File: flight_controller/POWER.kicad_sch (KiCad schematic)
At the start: 0 parts

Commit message: gps and power blocks
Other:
- note added: "15135-0801 cabel"
- note added: "JST B8B-PH-SM4-TBT(LF)(SN) CONN 8 PIN"
- note added: "MOLEX 5024430860 conn 8 pin"
- note added: "cabel ???"

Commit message: cleanup and improvements
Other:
- note added: "???"
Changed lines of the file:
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@@
+		)
+	)
+	(text "???"
+		(exclude_from_sim no)
+		(at 157.226 118.11 0)
+		(effects
+			(font
+				(size 1.27 1.27)
+			)
 		)
 	)
@@
 	(wire
 		(pts
+			(xy 123.19 123.19) (xy 158.75 123.19)
+		)
+		(stroke
+			(width 0)
+			(type default)
+			(color 255 0 0 1)
+		)
+	)
+	(wire
+		(pts
 			(xy 129.54 77.47) (xy 129.54 80.01)
 		)
@@
 			(width 0)
 			(type default)
+		)
+	)
+	(label "USB_TYPE_C_SENSE"
+		(at 132.08 123.19 0)
+		(effects
+			(font
+				(size 1.27 1.27)
+			)
+			(justify left bottom)
 		)
 	)
@@
 		(effects
 			(font
+				(size 1.27 1.27)
+			)
+			(justify left)
+		)
+	)
+	(hierarchical_label "USB_TYPE_C_SENSE"
+		(shape output)
+		(at 158.75 123.19 0)
+		(effects
+			(font

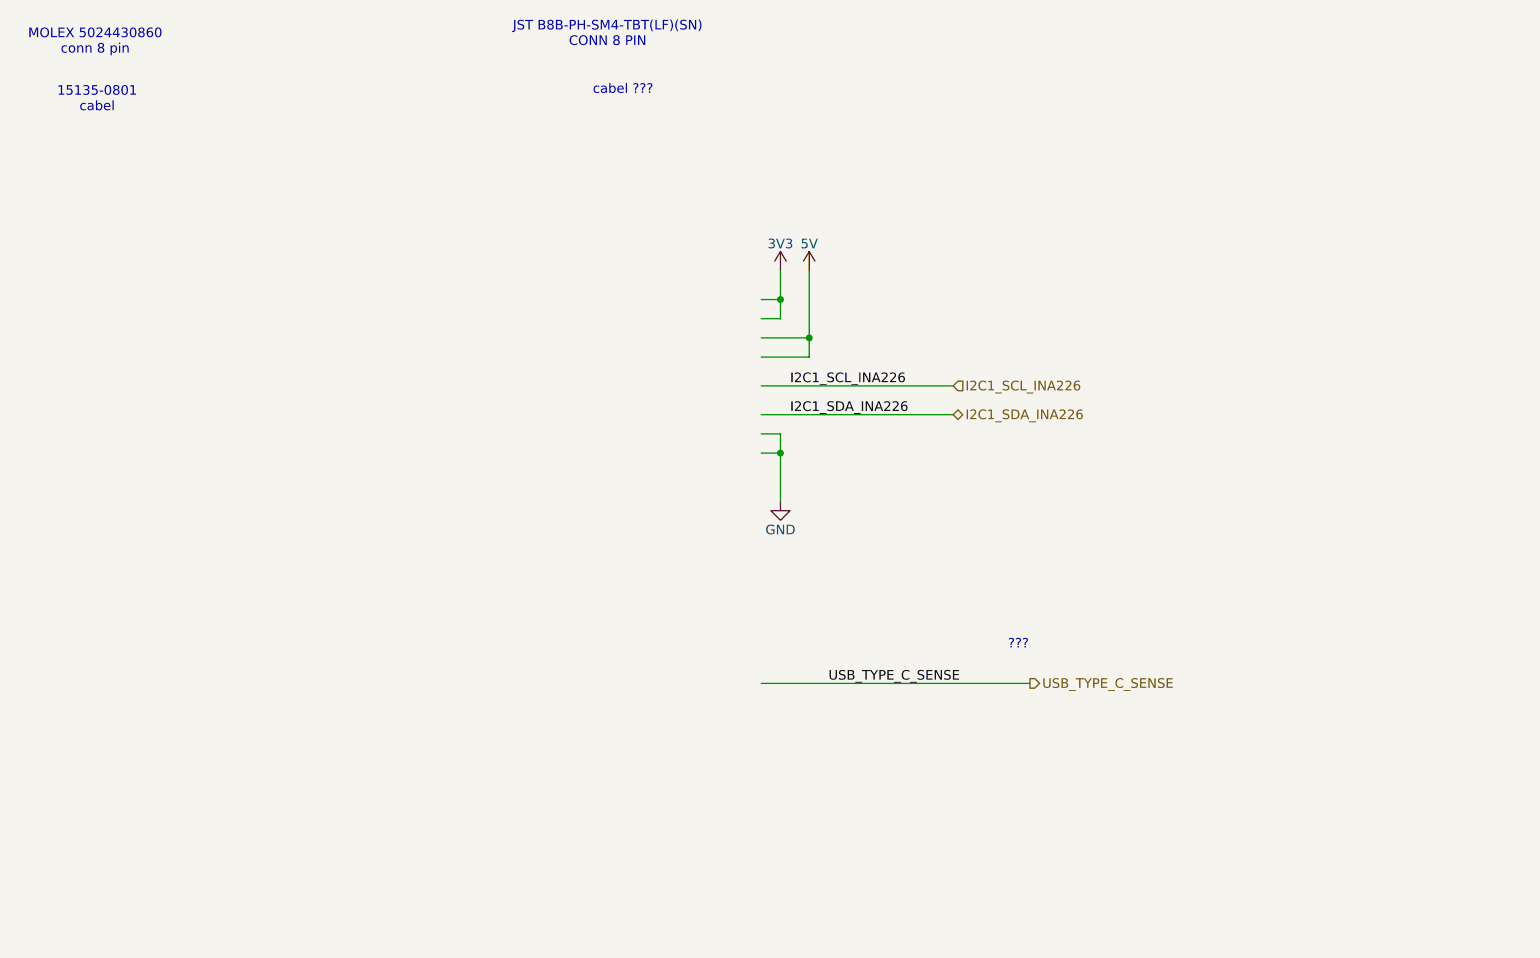
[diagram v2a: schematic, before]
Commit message: Schematic complete, ready for layout. Added USB, TPs, power conn, updated clocks, ran Rules Checker and general review
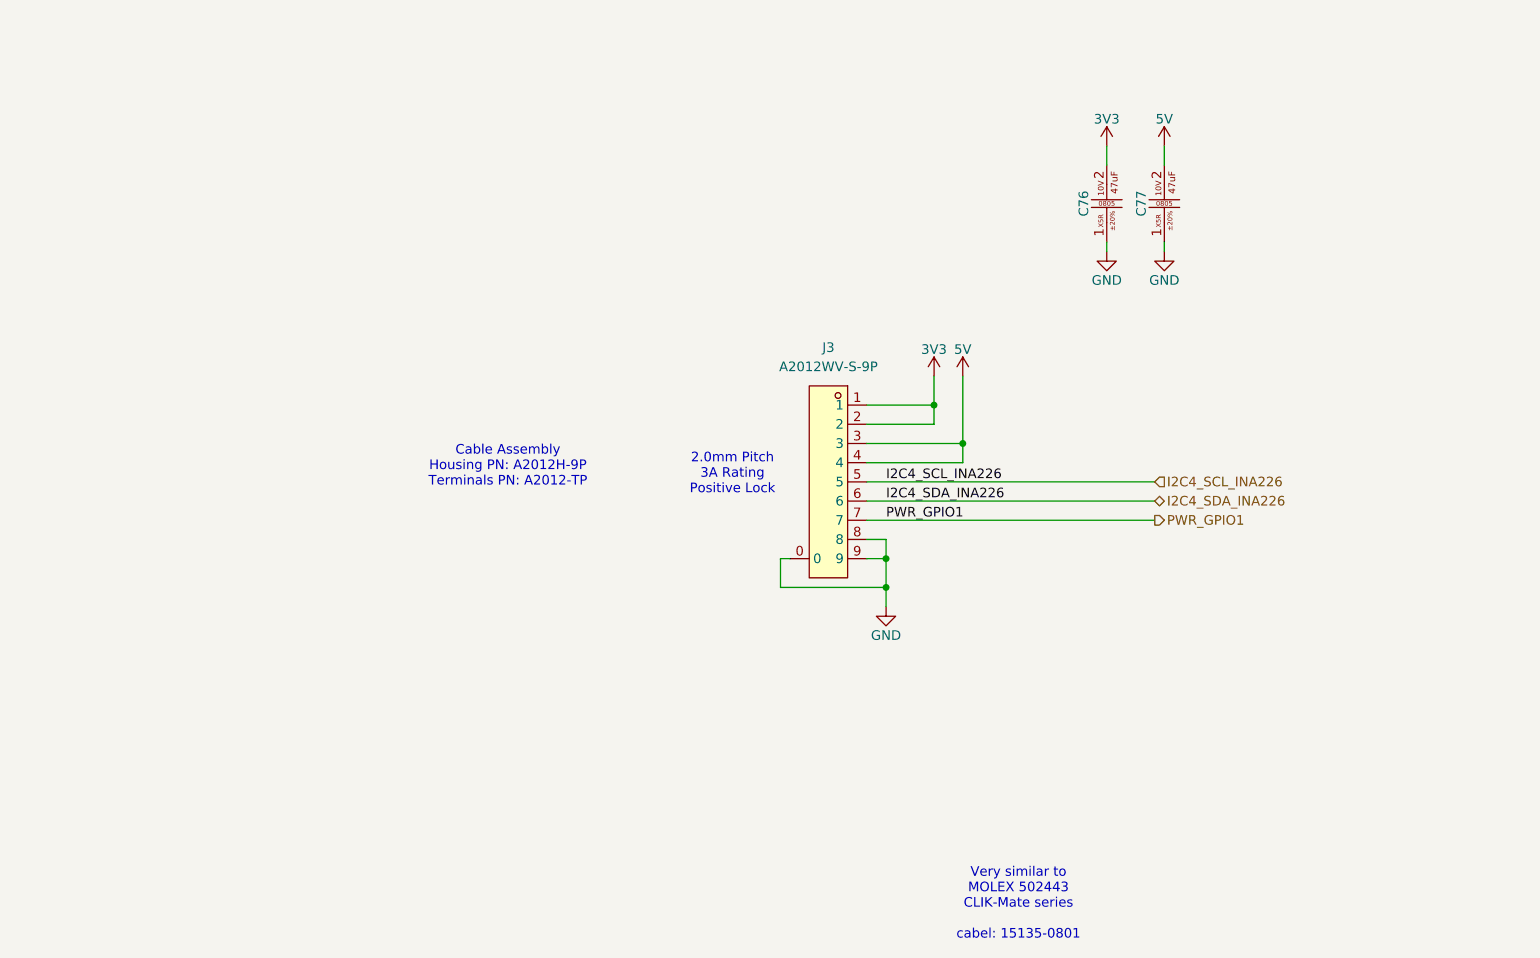
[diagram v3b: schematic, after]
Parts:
- added C76, C77: GRM21BR61A476ME15L (47uF , 0805 ,10V ,X5R), easyeda2kicad:C0805, symbol lampelKicadLIB:GRM21BR61A476ME15L (47uF , 0805 ,10V ,X5R)
- added J3: A2012WV-S-9P, easyeda2kicad:CONN-SMD_A2012WV-S-9P, symbol lampelKicadLIB:A2012WV-S-9P
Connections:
- net 3V3: now also C76.2, J3.1, J3.2
- net 5V: now also C77.2, J3.3, J3.4
- net GND: now also C76.1, C77.1, J3.0, J3.8, J3.9
- new net I2C4_SCL_INA226: J3.5
- new net I2C4_SDA_INA226: J3.6
- new net PWR_GPIO1: J3.7
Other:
- note added: "2.0mm Pitch 3A Rating Positive Lock"
- note added: "Cable Assembly Housing PN: A2012H-9P Terminals PN: A2012-TP"
- note added: "Very similar to MOLEX 502443 CLIK-Mate series cabel: 15135-0801"
- note removed: "15135-0801 cabel"
- note removed: "???"
- note removed: "JST B8B-PH-SM4-TBT(LF)(SN) CONN 8 PIN"
- note removed: "MOLEX 5024430860 conn 8 pin"
- note removed: "cabel ???"

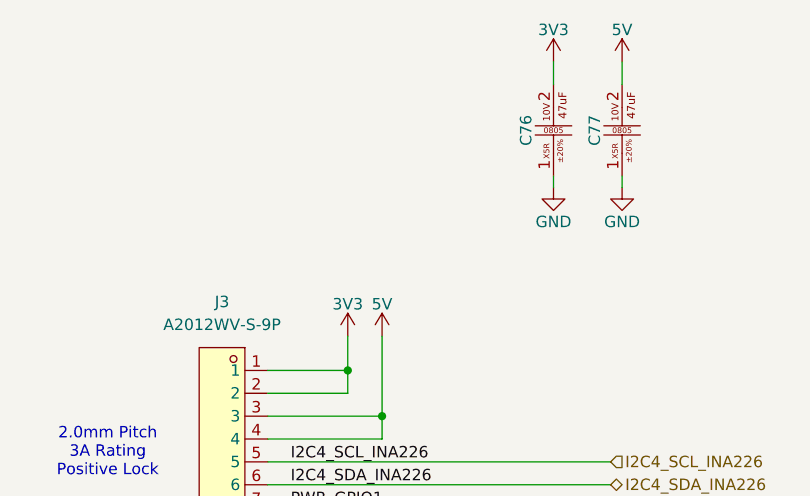
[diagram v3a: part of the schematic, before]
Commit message: Started the placement process
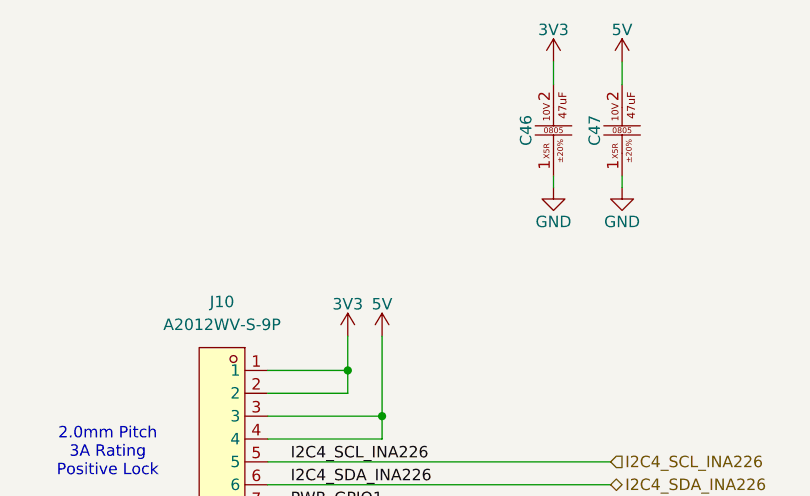
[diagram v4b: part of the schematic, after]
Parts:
- renumbered C76 to C46, C77 to C47, J3 to J10
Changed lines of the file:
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@@
 		(on_board yes)
 		(dnp no)
-		(property "Reference" "J3"
+		(property "Reference" "J10"
 			(at 132.08 78.74 0)
 			(effects
@@
 			(project ""
 				(path "/17737359-1a8e-4237-8899-d9604030bc1d/04e8a37e-c803-4b03-9bae-b305438bfc27"
-					(reference "J3")
+					(reference "J10")
 					(unit 1)
 				)
@@
 		(on_board yes)
 		(dnp no)
-		(property "Reference" "#PWR0128"
+		(property "Reference" "#PWR0118"
 			(at 139.7 119.38 0)
 			(effects
@@
 			(project "FP_BOARD"
 				(path "/17737359-1a8e-4237-8899-d9604030bc1d/04e8a37e-c803-4b03-9bae-b305438bfc27"
-					(reference "#PWR0128")
+					(reference "#PWR0118")
 					(unit 1)
 				)
@@
 		(dnp no)
 		(fields_autoplaced yes)
-		(property "Reference" "C77"
+		(property "Reference" "C47"
 			(at 173.482 59.69 0)
 			(do_not_autoplace yes)
@@
 			(project "FP_BOARD"
 				(path "/17737359-1a8e-4237-8899-d9604030bc1d/04e8a37e-c803-4b03-9bae-b305438bfc27"
-					(reference "C77")
+					(reference "C47")
 					(unit 1)
 				)
@@
 		(on_board yes)
 		(dnp no)
-		(property "Reference" "#PWR018"
+		(property "Reference" "#PWR0119"
 			(at 146.05 86.36 0)
 			(effects
@@
 			(project "FP_BOARD"
 				(path "/17737359-1a8e-4237-8899-d9604030bc1d/04e8a37e-c803-4b03-9bae-b305438bfc27"
-					(reference "#PWR018")
+					(reference "#PWR0119")
 					(unit 1)
 				)
@@
 		(on_board yes)
 		(dnp no)
-		(property "Reference" "#PWR085"
+		(property "Reference" "#PWR0120"
 			(at 149.86 86.36 0)
 			(effects
@@
 			(project "FP_BOARD"
 				(path "/17737359-1a8e-4237-8899-d9604030bc1d/04e8a37e-c803-4b03-9bae-b305438bfc27"
-					(reference "#PWR085")
+					(reference "#PWR0120")
 					(unit 1)
 				)
@@
 		(on_board yes)
 		(dnp no)
-		(property "Reference" "#PWR0134"
+		(property "Reference" "#PWR0124"
 			(at 176.53 72.39 0)
 			(effects
@@
 			(project "FP_BOARD"
 				(path "/17737359-1a8e-4237-8899-d9604030bc1d/04e8a37e-c803-4b03-9bae-b305438bfc27"
-					(reference "#PWR0134")
+					(reference "#PWR0124")
 					(unit 1)
 				)
@@
 		(dnp no)
 		(fields_autoplaced yes)
-		(property "Reference" "C76"
+		(property "Reference" "C46"
 			(at 165.862 59.69 0)
 			(do_not_autoplace yes)
@@
 			(project ""
 				(path "/17737359-1a8e-4237-8899-d9604030bc1d/04e8a37e-c803-4b03-9bae-b305438bfc27"
-					(reference "C76")
+					(reference "C46")
 					(unit 1)
 				)
@@
 		(on_board yes)
 		(dnp no)
-		(property "Reference" "#PWR0131"
+		(property "Reference" "#PWR0122"
 			(at 168.91 72.39 0)
 			(effects
@@
 			(project "FP_BOARD"
 				(path "/17737359-1a8e-4237-8899-d9604030bc1d/04e8a37e-c803-4b03-9bae-b305438bfc27"
-					(reference "#PWR0131")
+					(reference "#PWR0122")
 					(unit 1)
 				)
@@
 		(on_board yes)
 		(dnp no)
-		(property "Reference" "#PWR061"
+		(property "Reference" "#PWR0121"
 			(at 168.91 55.88 0)
 			(effects
@@
 			(project "FP_BOARD"
 				(path "/17737359-1a8e-4237-8899-d9604030bc1d/04e8a37e-c803-4b03-9bae-b305438bfc27"
-					(reference "#PWR061")
+					(reference "#PWR0121")
 					(unit 1)
 				)
@@
 		(on_board yes)
 		(dnp no)
-		(property "Reference" "#PWR0117"
+		(property "Reference" "#PWR0123"
 			(at 176.53 55.88 0)
 			(effects
@@
 			(project "FP_BOARD"
 				(path "/17737359-1a8e-4237-8899-d9604030bc1d/04e8a37e-c803-4b03-9bae-b305438bfc27"
-					(reference "#PWR0117")
-					(unit 1)
-				)
+					(reference "#PWR0123")
+					(unit 1)
+				)

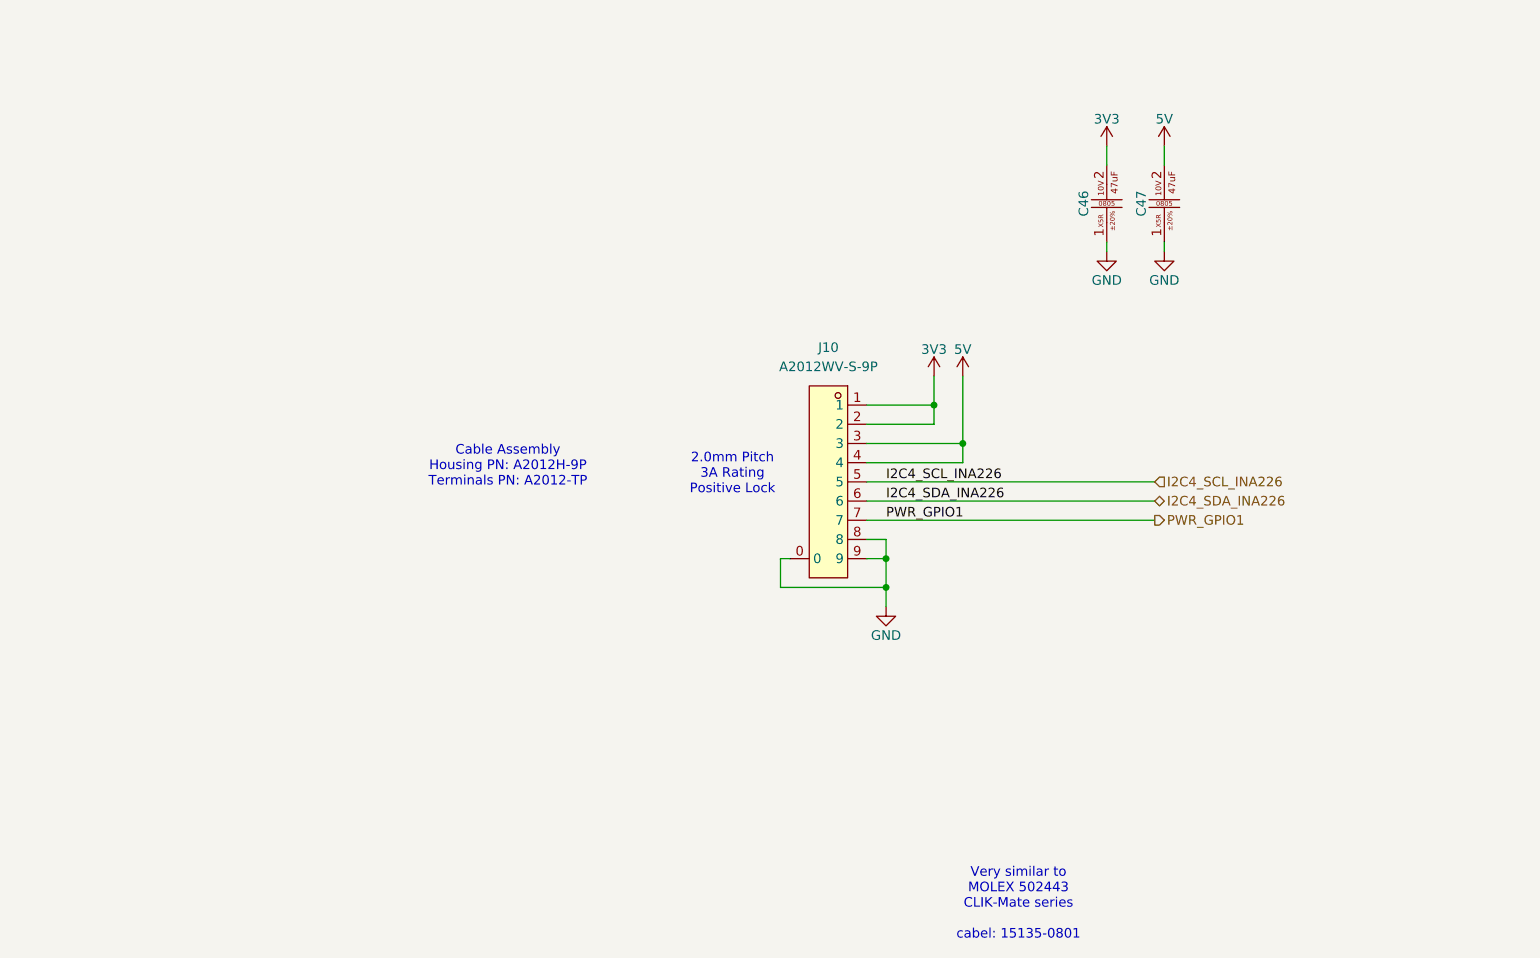
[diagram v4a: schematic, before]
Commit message: Updated power and usb connectors, annotations and netlist check
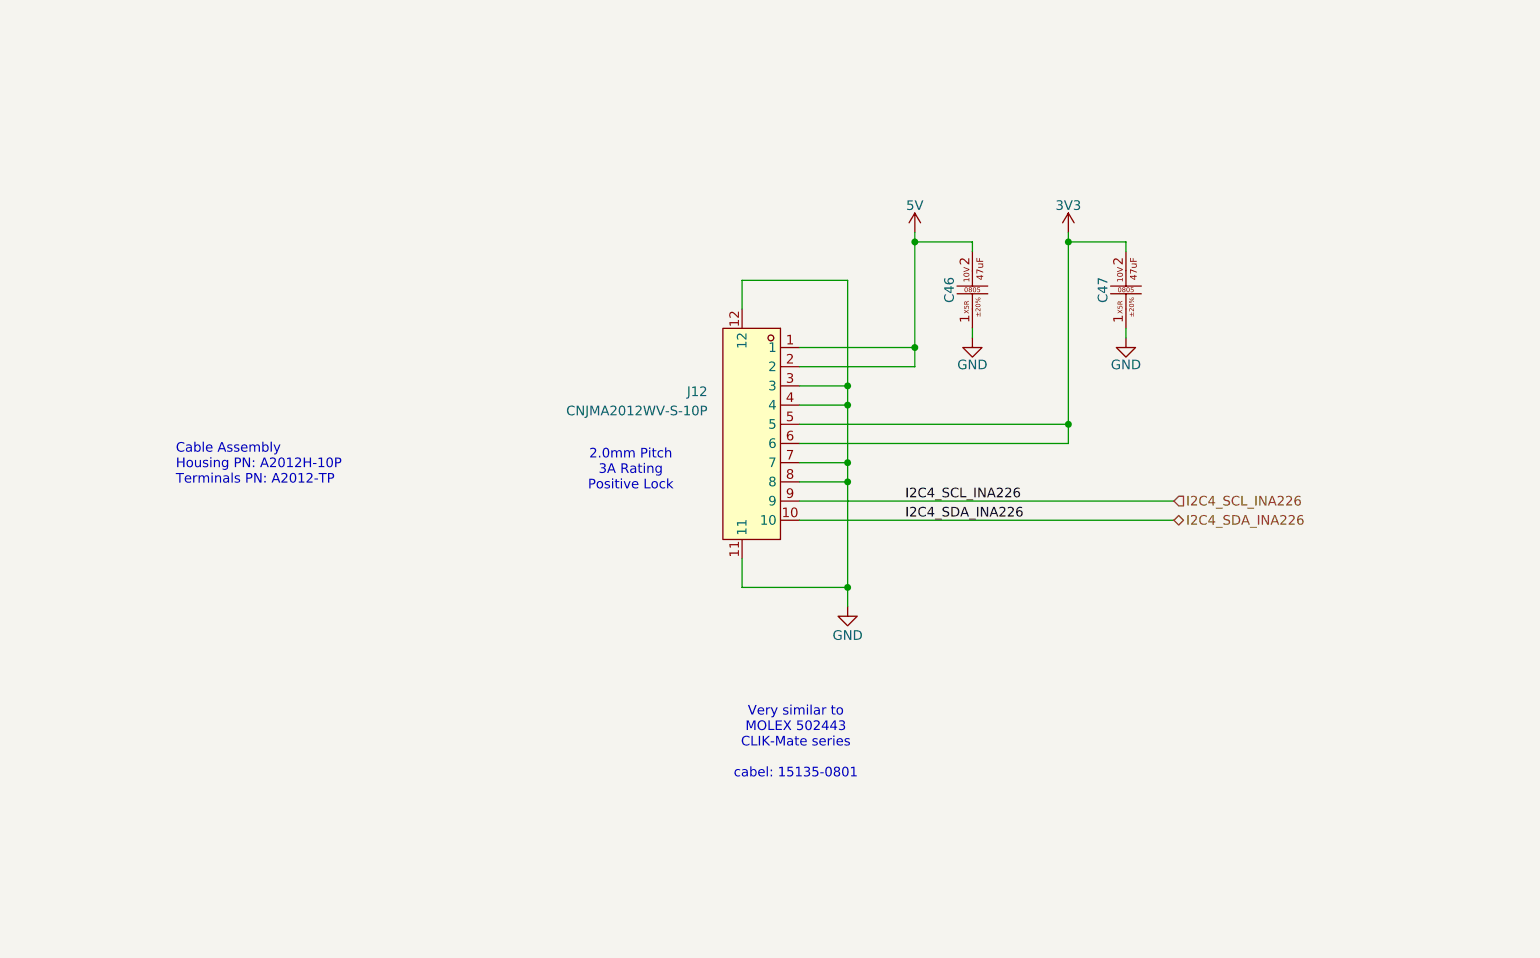
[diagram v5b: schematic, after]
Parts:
- removed J10: A2012WV-S-9P, easyeda2kicad:CONN-SMD_A2012WV-S-9P, symbol lampelKicadLIB:A2012WV-S-9P
- added J12: CNJMA2012WV-S-10P, easyeda2kicad:CONN-SMD_10P-P1.25_CNJM_CNJMA2012WV-S-10P, symbol lampelKicadLIB:CNJMA2012WV-S-10P
- renumbered C47 to C46, C46 to C47
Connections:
- net 3V3: now also J12.5, J12.6
- net 5V: now also J12.1, J12.2
- net GND: now also J12.11, J12.12, J12.3, J12.4, J12.7, J12.8
- net I2C4_SCL_INA226: now also J12.9
- net I2C4_SDA_INA226: now also J12.10
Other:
- note added: "Cable Assembly Housing PN: A2012H-10P Terminals PN: A2012-TP"
- note removed: "Cable Assembly Housing PN: A2012H-9P Terminals PN: A2012-TP"
- moved on the sheet: C46, C47
